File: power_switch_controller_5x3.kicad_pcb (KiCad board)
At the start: 2 copper layers, 120.7 x 66 mm, 1 part

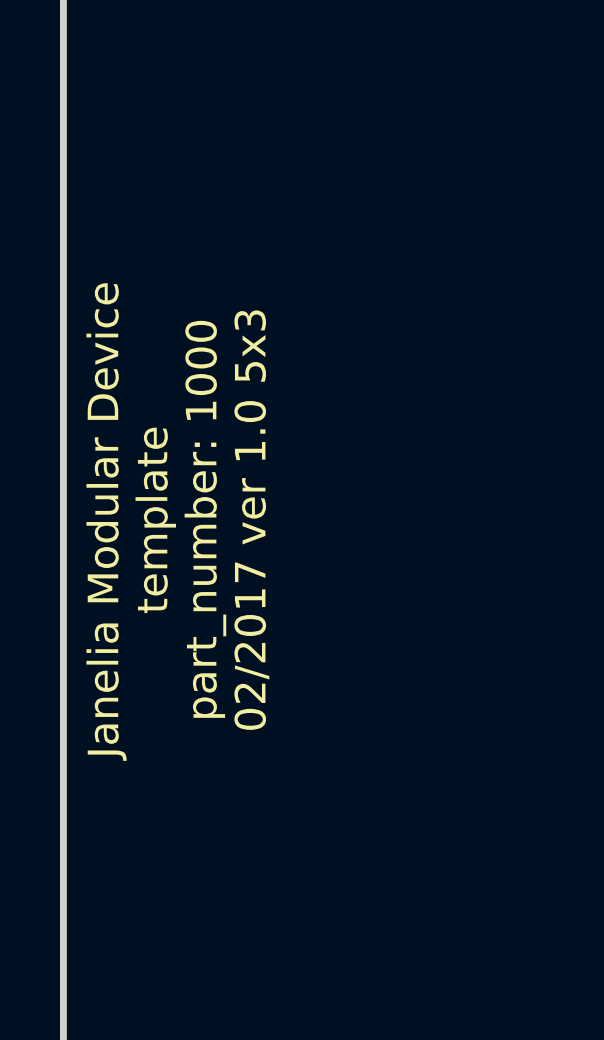
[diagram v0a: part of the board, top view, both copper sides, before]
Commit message: template -> power_switch_controller.
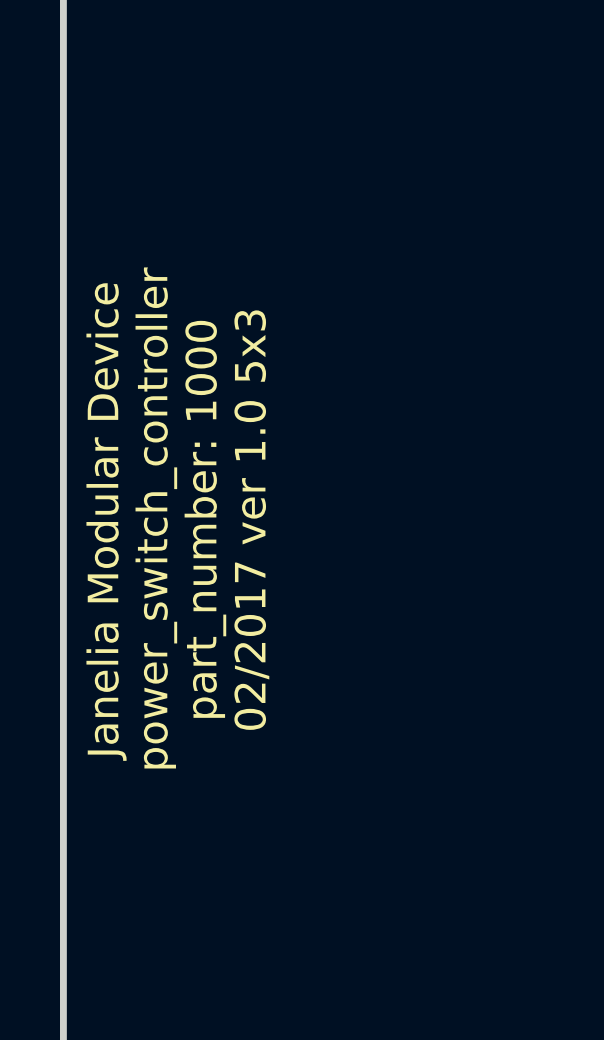
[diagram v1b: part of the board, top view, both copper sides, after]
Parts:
- MDB1: footprint template_5x3:MODULAR_DEVICE_BASE_5X3_MALE -> power_switch_controller_5x3:MODULAR_DEVICE_BASE_5X3_MALE
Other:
- board text added: "Janelia Modular Device power_switch_controller part_number: 1000 02/2017 ver 1.0 5x3"
- board text removed: "Janelia Modular Device template part_number: 1000 02/2017 ver 1.0 5x3"
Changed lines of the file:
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@@
   (page A4)
   (title_block
-    (title template_5x3)
+    (title power_switch_controller_5x3)
     (rev 1.0)
   )
@@
     (diff_pair_width 0.254)
   )
-  (module template_5x3:MODULAR_DEVICE_BASE_5X3_MALE (layer F.Cu)
+  (module power_switch_controller_5x3:MODULAR_DEVICE_BASE_5X3_MALE (layer F.Cu)
     (at 91.44 105.41)
     (fp_text reference MDB1 (at 0 0) (layer F.SilkS) hide
@@
     (effects (font (size 1.016 1.016) (thickness 0.1905)))
   )
-  (gr_text "Janelia Modular Device\ntemplate\npart_number: 1000\n02/2017 ver 1.0 5x3" (at 73.66 105.41 90) (layer F.SilkS)
+  (gr_text "Janelia Modular Device\npower_switch_controller\npart_number: 1000\n02/2017 ver 1.0 5x3" (at 73.66 105.41 90) (layer F.SilkS)
     (effects (font (size 1.016 1.016) (thickness 0.254)))
   )

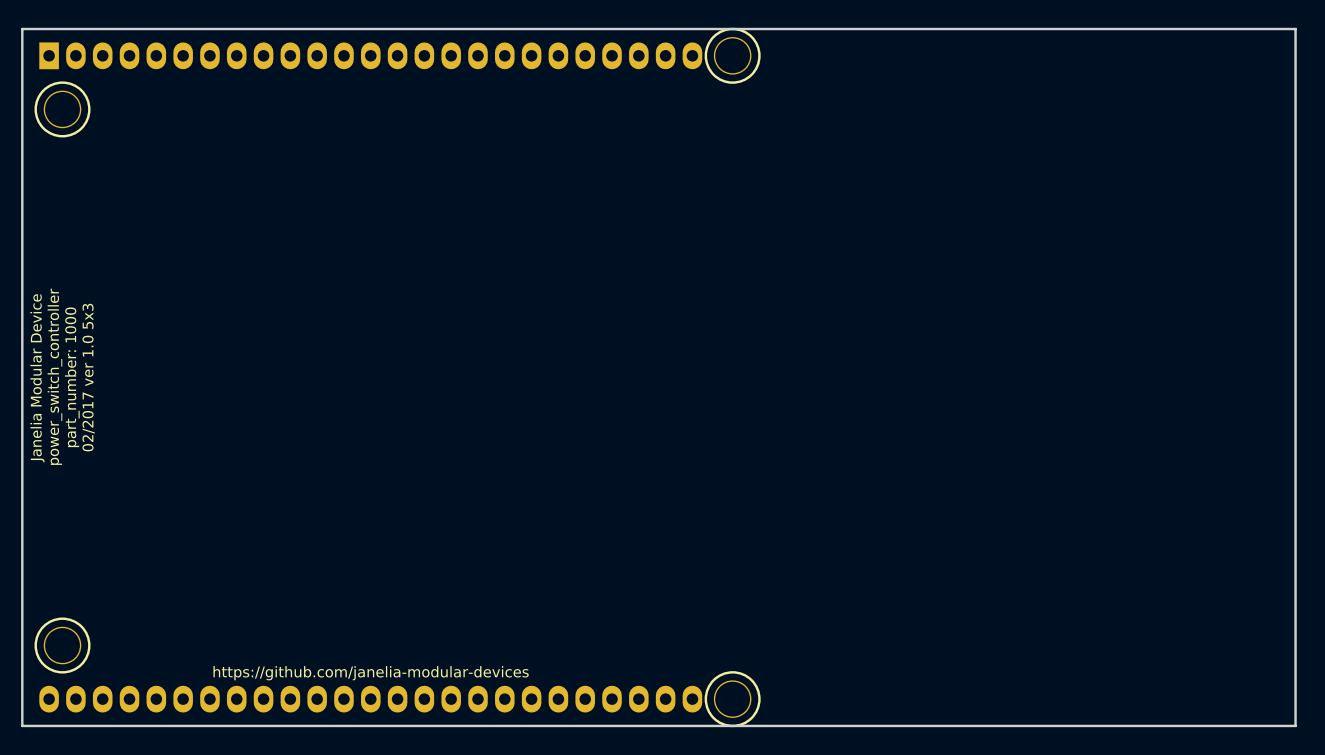
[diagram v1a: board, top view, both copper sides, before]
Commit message: Moved edge positions.
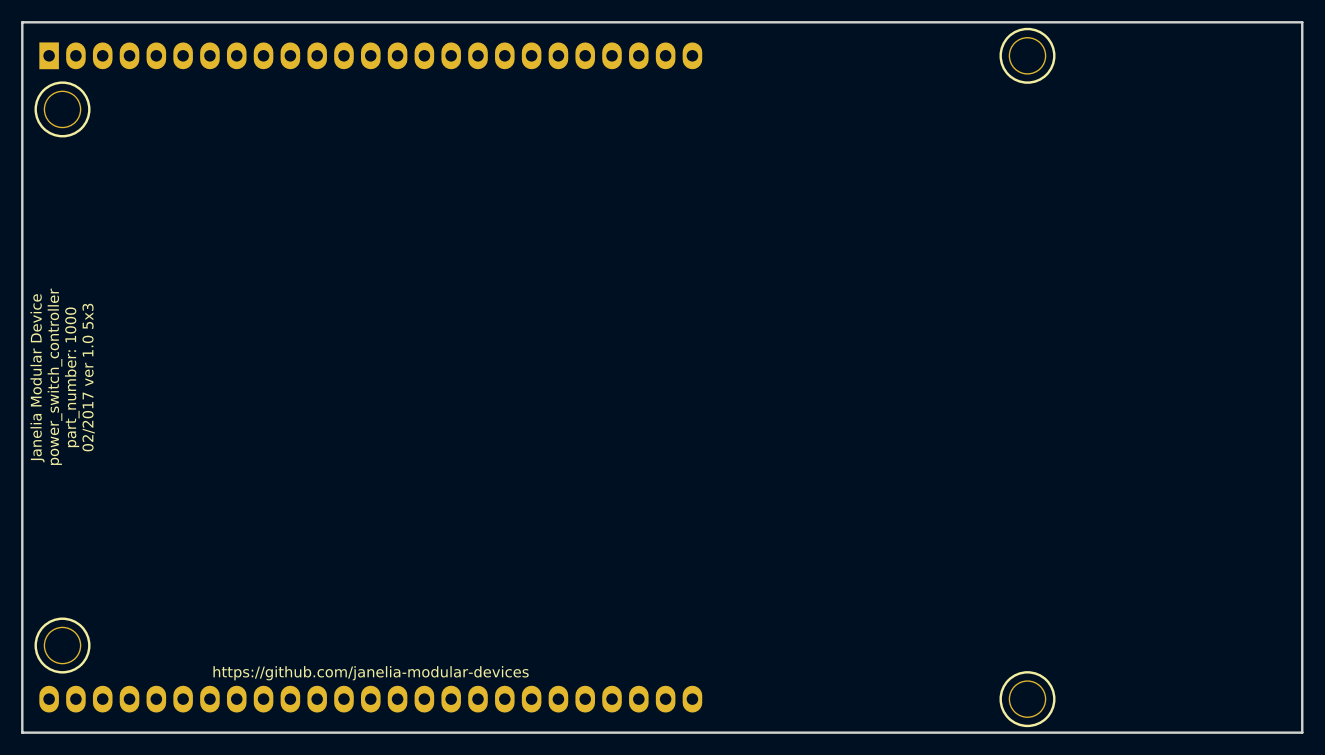
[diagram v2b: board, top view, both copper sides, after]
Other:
- board size 120.7 x 66 mm -> 121.3 x 67.3 mm
